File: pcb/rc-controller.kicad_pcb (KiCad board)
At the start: 2 copper layers, 203.2 x 78.7 mm, 77 parts, among them J1 USB_C_Receptacle_USB2.0, M1 Motor_DC, Q1 AO3401A, Q2 AO3401A, Q3 AO3400A, Q4 AO3400A, SW1 SW_SPDT, SW2 SW_SPDT, SW3 SW_Push, SW4 SW_Push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

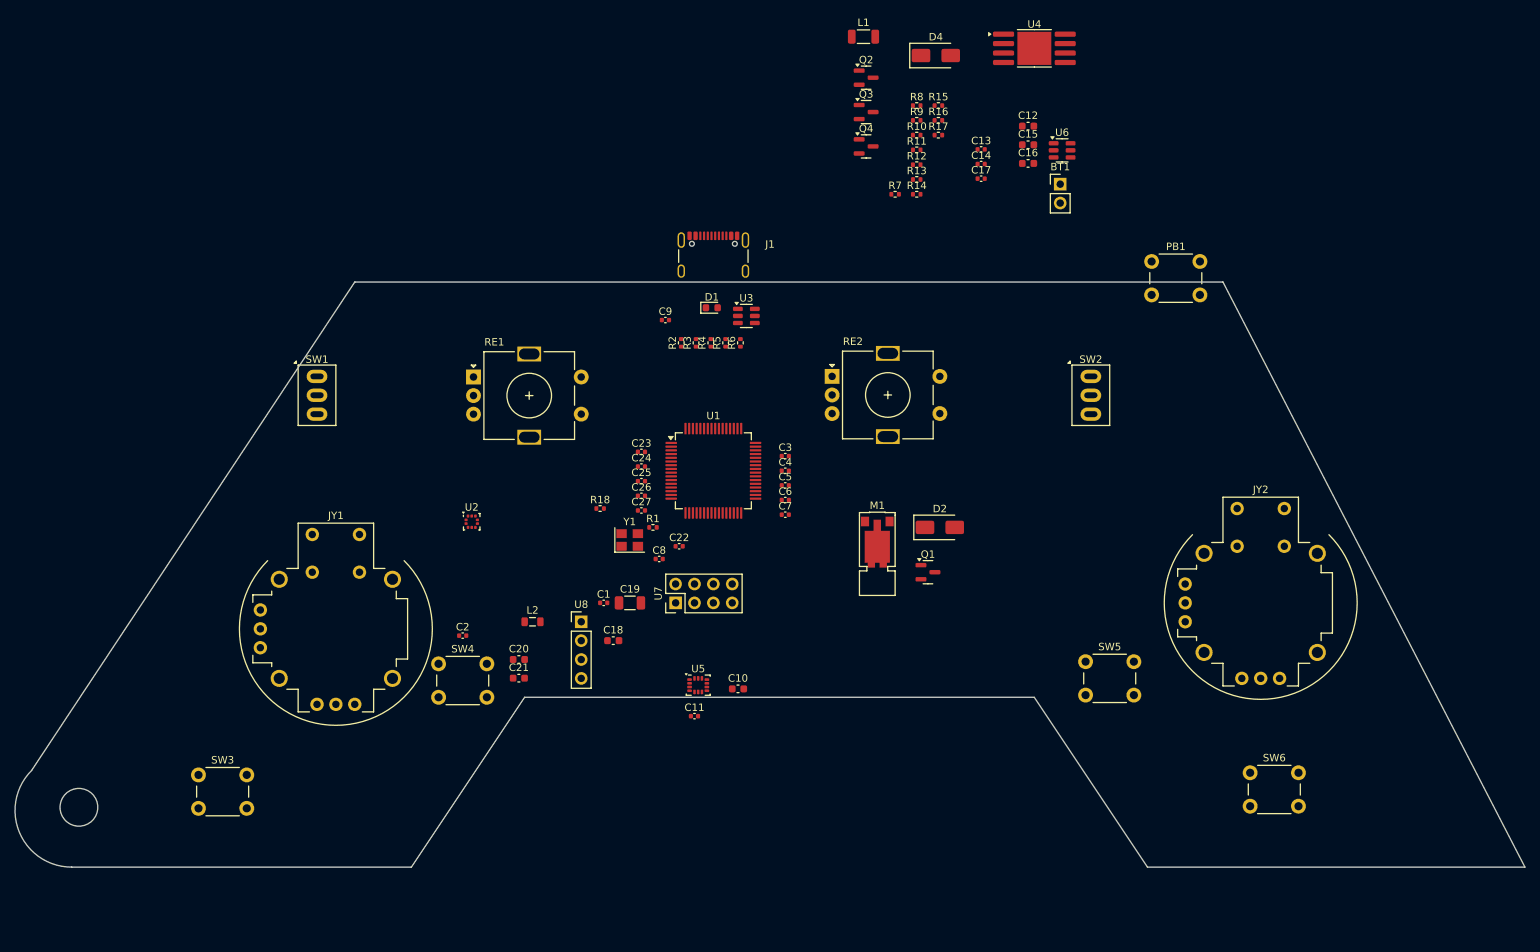
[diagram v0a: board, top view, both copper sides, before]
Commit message: Finish rough layout
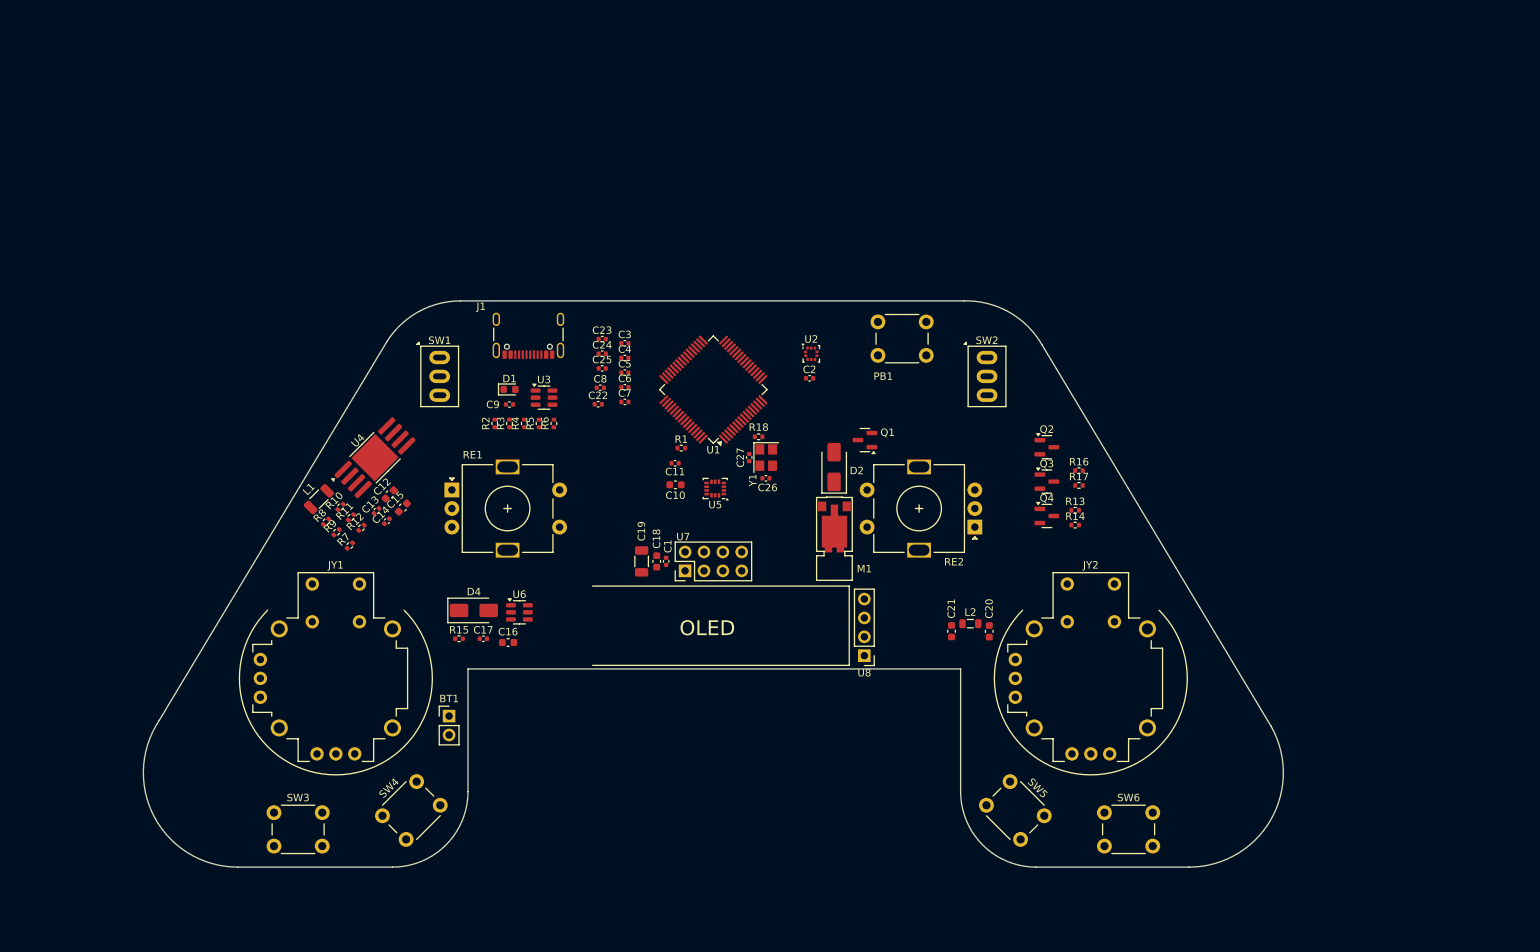
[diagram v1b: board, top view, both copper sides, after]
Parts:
- moved BT1 109.0 mm to (101.6, 116.8)
- moved U4 104.4 mm to (91.6, 82.1), turned to 45 degrees
- moved C12 99.2 mm to (93.6, 87.0), turned to 45 degrees
- moved C15 97.3 mm to (95.4, 88.8), turned to 45 degrees
- moved R8 97.2 mm to (85.0, 90.7), turned to 45 degrees
- moved D4 97.2 mm to (104.9, 102.6)
- moved R15 96.5 mm to (102.9, 106.4)
- moved L1 96.1 mm to (84.1, 87.6), turned to 45 degrees
- moved U6 95.9 mm to (111.1, 102.9)
- moved R9 95.8 mm to (86.4, 92.1), turned to 45 degrees
- moved C16 95.1 mm to (109.5, 106.9)
- moved C13 94.8 mm to (91.8, 89.2), turned to 45 degrees
- moved C14 93.3 mm to (93.2, 90.6), turned to 45 degrees
- moved R10 92.3 mm to (87.0, 88.7), turned to 45 degrees
- moved C17 91.2 mm to (106.2, 106.4)
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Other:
- board size 203.2 x 78.7 mm -> 153.4 x 76.2 mm
- board text added: "BATT"
- board text added: "OLED"

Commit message: Final placement before routing
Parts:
- removed J1: USB_C_Receptacle_USB2.0, Connector_USB:USB_C_Receptacle_GCT_USB4105-xx-A_16P_TopMnt_Horizontal
- added C28: 10u, Capacitor_SMD:C_0402_1005Metric, F.Cu at (134.2, 82.8)
- added J2: USB_C_Receptacle_USB2.0_16P, Connector_USB:USB_C_Receptacle_GCT_USB4105-xx-A_16P_TopMnt_Horizontal, F.Cu at (112.2, 64.5)
- added JP1: Jumper_2_Open, Jumper:SolderJumper-2_P1.3mm_Open_RoundedPad1.0x1.5mm, F.Cu at (98.1, 79.8)
- moved R17 81.2 mm to (105.4, 79.8)
- moved R16 81.0 mm to (105.4, 81.0), turned to 180 degrees
- moved R13 35.2 mm to (157.0, 69.0), turned to 90 degrees
- moved C25 24.7 mm to (146.0, 76.8), turned to -90 degrees
- moved R14 24.3 mm to (168.0, 74.6)
- moved Q2 24.2 mm to (159.4, 72.0), turned to -90 degrees
- moved C24 24.2 mm to (144.8, 76.8), turned to -90 degrees
- moved C3 23.7 mm to (145.4, 79.2)
- moved Q4 23.3 mm to (167.2, 72.0), turned to 90 degrees
- moved Q3 22.9 mm to (163.3, 72.0), turned to 90 degrees
- moved C22 22.8 mm to (141.2, 63.2), turned to 180 degrees
- moved C7 20.7 mm to (145.3, 69.4)
- moved C8 20.2 mm to (139.8, 82.0), turned to -90 degrees
- moved C23 19.1 mm to (141.2, 64.4), turned to 180 degrees
- moved C6 16.8 mm to (139.2, 63.2)
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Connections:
- net Net-(U1-VCAP1) renamed /VCAP
- net Net-(U1-VREF+) renamed /VREF
- JY1 pad B1: /JY1SW -> GND
- JY1 pad H1: /JY1Y -> (no net)
- JY1 pad H2: +3V3 -> (no net)
- JY1 pad H3: GND -> (no net)
- JY1 pad S1: GND -> /JY1SW
- JY1 pad V1: /JY1X -> (no net)
- JY1 pad V2: +3V3 -> (no net)
- JY1 pad V3: GND -> (no net)
- JY2 pad B1: /JY2SW -> GND
- JY2 pad H1: /JY2Y -> (no net)
- JY2 pad H2: +3V3 -> (no net)
- JY2 pad H3: GND -> (no net)
- JY2 pad S1: GND -> /JY2SW
- JY2 pad V1: /JY2X -> (no net)
- JY2 pad V2: +3V3 -> (no net)
- JY2 pad V3: GND -> (no net)
- U5 pad 9: /GINT2 -> unconnected-(U5-INT2-Pad9)
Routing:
- net /USB_D-: track 0.00 -> 2.77 mm
- net /USB_D+: track 0.00 -> 2.64 mm
- net Net-(JP1-B): track 0.00 -> 1.66 mm, vias 0 -> 1

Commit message: Add net classes for pcb
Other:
- rule pad_to_mask_clearance: 0 -> 0.038
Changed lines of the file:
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@@
 	)
 	(setup
-		(pad_to_mask_clearance 0)
-		(allow_soldermask_bridges_in_footprints no)
+		(stackup
+			(layer "F.SilkS"
+				(type "Top Silk Screen")
+			)
+			(layer "F.Paste"
+				(type "Top Solder Paste")
+			)
+			(layer "F.Mask"
+				(type "Top Solder Mask")
+				(thickness 0.01)
+			)
+			(layer "F.Cu"
+				(type "copper")
+				(thickness 0.035)
+			)
+			(layer "dielectric 1"
+				(type "core")
+				(thickness 1.51)
+				(material "FR4")
+				(epsilon_r 4.5)
+				(loss_tangent 0.02)
+			)
+			(layer "B.Cu"
+				(type "copper")
+				(thickness 0.035)
+			)
+			(layer "B.Mask"
+				(type "Bottom Solder Mask")
+				(thickness 0.01)
+			)
+			(layer "B.Paste"
+				(type "Bottom Solder Paste")
+			)
+			(layer "B.SilkS"
+				(type "Bottom Silk Screen")
+			)
+			(copper_finish "HAL SnPb")
+			(dielectric_constraints no)
+		)
+		(pad_to_mask_clearance 0.038)
+		(solder_mask_min_width 0.1)
+		(allow_soldermask_bridges_in_footprints yes)
 		(pcbplotparams
 			(layerselection 0x00010fc_ffffffff)
@@
 		(tags "resistor")
 		(property "Reference" "R17"
-			(at -1.8 0 360)
+			(at -1.8 0 0)
 			(layer "F.SilkS")
 			(effects
@@
 		)
 		(property "Value" "200k"
-			(at 0 1.17 360)
+			(at 0 1.17 0)
 			(layer "F.Fab")
 			(effects
@@
 		)
 		(fp_text user "${REFERENCE}"
-			(at 0 0 360)
+			(at 0 0 0)
 			(layer "F.Fab")
 			(effects
@@
 		)
 		(property "Value" "AO3400A"
-			(at 0 2.4 270)
+			(at 0 2.4 -90)
 			(layer "F.Fab")
 			(effects
@@
 		)
 		(fp_text user "${REFERENCE}"
-			(at 0 0 270)
+			(at 0 0 -90)
 			(layer "F.Fab")
 			(effects
@@
 		(tags "resistor")
 		(property "Reference" "R3"
-			(at 1.6 0 360)
+			(at 1.6 0 0)
 			(layer "F.SilkS")
 			(effects
@@
 		)
 		(property "Value" "10k"
-			(at 0 1.17 360)
+			(at 0 1.17 0)
 			(layer "F.Fab")
 			(effects
@@
 		)
 		(fp_text user "${REFERENCE}"
-			(at 0 0 360)
+			(at 0 0 0)
 			(layer "F.Fab")
 			(effects
@@
 		(tags "resistor")
 		(property "Reference" "R1"
-			(at -1.6 0 360)
+			(at -1.6 0 0)
 			(layer "F.SilkS")
 			(effects
@@
 		)
 		(property "Value" "10k"
-			(at 0 1.17 360)
+			(at 0 1.17 0)
 			(layer "F.Fab")
 			(effects
@@
 		)
 		(fp_text user "${REFERENCE}"
-			(at 0 0 360)
+			(at 0 0 0)
 			(layer "F.Fab")
 			(effects
@@
 		(tags "capacitor")
 		(property "Reference" "C6"
-			(at 0 -0.8 360)
+			(at 0 -0.8 0)
 			(layer "F.SilkS")
 			(effects
@@
 		)
 		(property "Value" "100n"
-			(at 0 1.16 360)
+			(at 0 1.16 0)
 			(layer "F.Fab")
 			(effects
@@
 		)
 		(fp_text user "${REFERENCE}"
-			(at 0 0 360)
+			(at 0 0 0)
 			(layer "F.Fab")
 			(effects
@@
 		(tags "resistor")
 		(property "Reference" "R13"
-			(at 0 -1 270)
+			(at 0 -1 -90)
 			(layer "F.SilkS")
 			(effects
@@
 		)
 		(property "Value" "47k"
-			(at 0 1.17 270)
+			(at 0 1.17 -90)
 			(layer "F.Fab")
 			(effects
@@
 		)
 		(fp_text user "${REFERENCE}"
-			(at 0 0 270)
+			(at 0 0 -90)
 			(layer "F.Fab")
 			(effects
@@
 		)
 		(property "Value" "10u"
-			(at 0 1.43 270)
+			(at 0 1.43 -90)
 			(layer "F.Fab")
 			(effects
@@
 		)
 		(fp_text user "${REFERENCE}"
-			(at 0 0 270)
+			(at 0 0 -90)
 			(layer "F.Fab")
 			(effects
@@
 		(tags "LED")
 		(property "Reference" "D1"
-			(at -2.128 -0.075001 270)
+			(at -2.128 -0.075001 -90)
 			(layer "F.SilkS")
 			(effects
@@
 		)
 		(property "Value" "LEDB"
-			(at 0 1.43 270)
+			(at 0 1.43 -90)
 			(layer "F.Fab")
 			(effects
@@
 		)
 		(fp_text user "${REFERENCE}"
-			(at 0 0 270)
+			(at 0 0 -90)
 			(layer "F.Fab")
 			(effects
@@
 		)
 		(property "Value" "AO3400A"
-			(at 0 2.4 270)
+			(at 0 2.4 -90)
 			(layer "F.Fab")
 			(effects
@@
 		)
 		(fp_text user "${REFERENCE}"
-			(at 0 0 270)
+			(at 0 0 -90)
 			(layer "F.Fab")
 			(effects
@@
 		(tags "capacitor")
 		(property "Reference" "C12"
-			(at 1 1.2 315)
+			(at 1 1.2 -45)
 			(layer "F.SilkS")
 			(effects
@@
 		)
 		(property "Value" "22u"
-			(at 0 1.43 270)
+			(at 0 1.43 -90)
 			(layer "F.Fab")
 			(effects
@@
 		)
 		(fp_text user "${REFERENCE}"
-			(at 0 0 270)
+			(at 0 0 -90)
 			(layer "F.Fab")
 			(effects
@@
 		)
 		(property "Value" "SS24"
-			(at 0 2.600001 270)
+			(at 0 2.600001 -90)
 			(layer "F.Fab")
 			(effects
@@
 		)
 		(fp_text user "${REFERENCE}"
-			(at 0 -2.5 270)
+			(at 0 -2.5 -90)
 			(layer "F.Fab")
 			(effects
@@
 		(tags "capacitor")
 		(property "Reference" "C3"
-			(at 0 -1 360)
+			(at 0 -1 0)
 			(layer "F.SilkS")
 			(effects
@@
 		)
 		(property "Value" "100n"
-			(at 0 1.16 360)
+			(at 0 1.16 0)
 			(layer "F.Fab")
 			(effects
@@
 		)
 		(fp_text user "${REFERENCE}"
-			(at 0 0 360)
+			(at 0 0 0)
 			(layer "F.Fab")
 			(effects
@@
 		(tags "solder jumper open")
 		(property "Reference" "JP1"
-			(at 2.2 0 225)
+			(at 2.2 0 -135)
 			(layer "F.SilkS")
 			(effects
@@
 		(fp_arc
 			(start -0.7 1)
-			(mid -1.194976 0.794975)
+			(mid -1.194977 0.794976)
 			(end -1.4 0.300001)
 			(stroke
@@
 		)
 		(property "Value" "22u"
-			(at 0 1.43 270)
+			(at 0 1.43 -90)
 			(layer "F.Fab")
 			(effects
@@
 		)
 		(fp_text user "${REFERENCE}"
-			(at 0 0 270)
+			(at 0 0 -90)
 			(layer "F.Fab")
 			(effects
@@
 		(tags "resistor")
 		(property "Reference" "R5"
-			(at 1.6 0 360)
+			(at 1.6 0 0)
 			(layer "F.SilkS")
 			(effects
@@
 		)
 		(property "Value" "5k1"
-			(at 0 1.17 360)
+			(at 0 1.17 0)
 			(layer "F.Fab")
 			(effects
@@
 		)
 		(fp_text user "${REFERENCE}"
-			(at 0 0 360)
+			(at 0 0 0)
 			(layer "F.Fab")
 			(effects
